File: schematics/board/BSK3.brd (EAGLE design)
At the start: 82 x 100 mm, 19 parts

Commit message: Новые схемы
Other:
- board text added: "BSK3 "Концерн ИТС""
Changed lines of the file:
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@@
 <circle x="41" y="50" radius="16.375" width="2.25" layer="29"/>
 <rectangle x1="10.528" y1="39.862" x2="22.528" y2="56.862" layer="29"/>
-<text x="18.8" y="74" size="1.4224" layer="26" rot="MR0">BUS+</text>
-<text x="68.2" y="74.1" size="1.4224" layer="26" rot="MR0">BUS+</text>
-<text x="68.1" y="24.5" size="1.4224" layer="26" rot="MR0">BUS+</text>
-<text x="18.7" y="24.4" size="1.4224" layer="26" rot="MR0">BUS+</text>
-<text x="27" y="65.6" size="1.4224" layer="26" rot="MR0">BUS-</text>
-<text x="59.6" y="65.5" size="1.4224" layer="26" rot="MR0">BUS-</text>
-<text x="59.6" y="33.2" size="1.4224" layer="26" rot="MR0">BUS-</text>
-<text x="27" y="33" size="1.4224" layer="26" rot="MR0">BUS-</text>
+<text x="13.9" y="68.7" size="1.4224" layer="25" rot="MR45">BUS+</text>
+<text x="72.3" y="72.8" size="1.4224" layer="26" rot="MR315">BUS+</text>
+<text x="60.3" y="24.2" size="1.4224" layer="26" rot="MR225">BUS+</text>
+<text x="17.7" y="20.1" size="1.4224" layer="26" rot="MR135">BUS+</text>
+<text x="22.7" y="60.1" size="1.4224" layer="26" rot="MR45">BUS-</text>
+<text x="62.2" y="62.9" size="1.4224" layer="26" rot="MR315">BUS-</text>
+<text x="52.3" y="32.3" size="1.4224" layer="26" rot="MR225">BUS-</text>
+<text x="26.2" y="28.6" size="1.4224" layer="26" rot="MR135">BUS-</text>
+<text x="80.7" y="41.3" size="1.778" layer="25" rot="R90">BSK3 "Концерн ИТС"</text>
 </plain>
 <attributes>

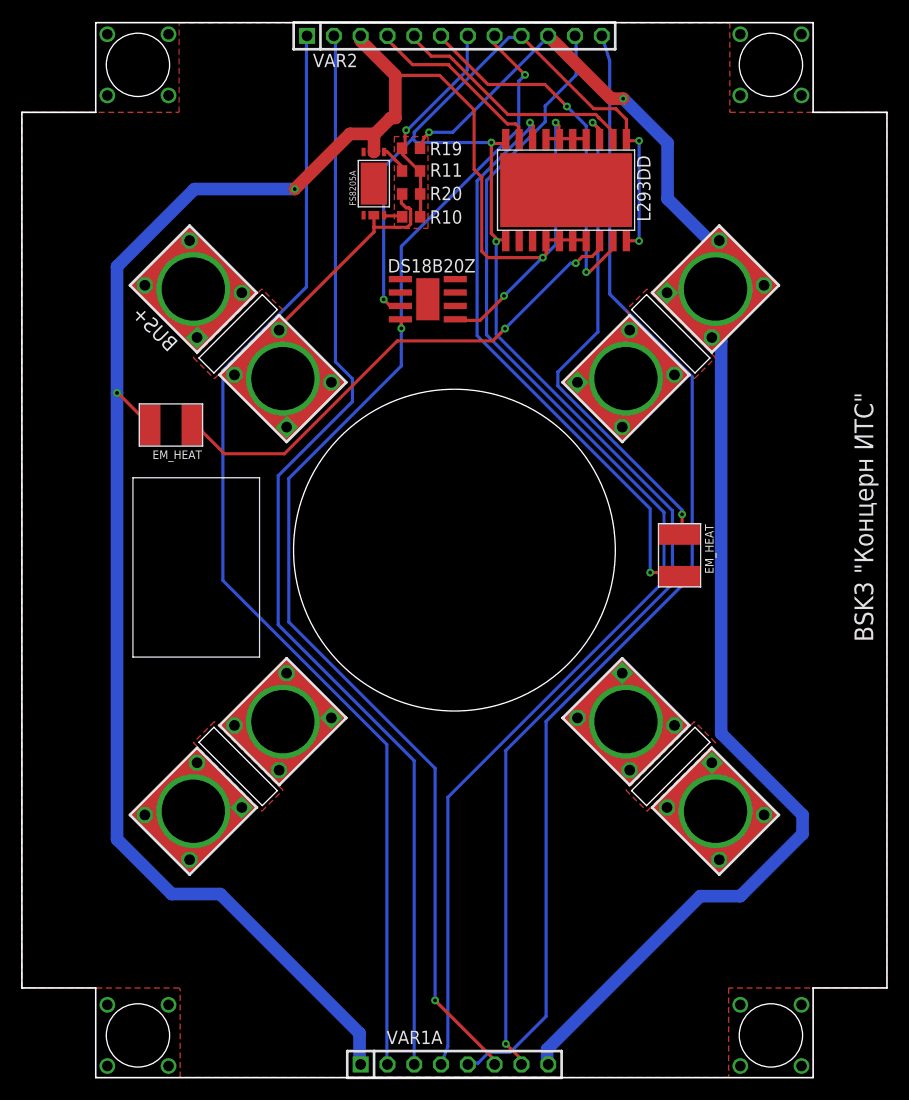
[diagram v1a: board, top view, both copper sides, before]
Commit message: изменен БСК4
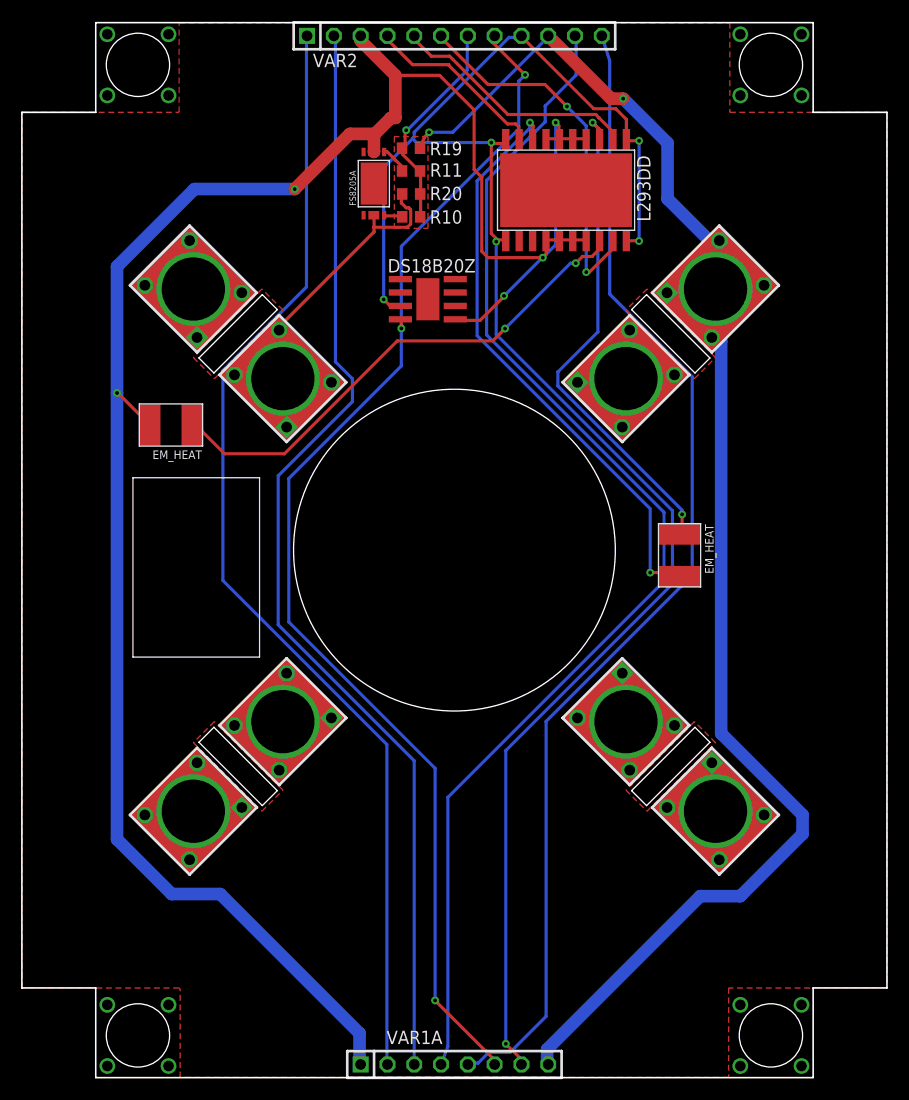
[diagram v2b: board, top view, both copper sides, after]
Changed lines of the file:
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@@
 <circle x="41" y="50" radius="16.375" width="2.25" layer="29"/>
 <rectangle x1="10.528" y1="39.862" x2="22.528" y2="56.862" layer="29"/>
-<text x="13.9" y="68.7" size="1.4224" layer="25" rot="MR45">BUS+</text>
+<text x="13.9" y="68.7" size="1.4224" layer="26" rot="MR45">BUS+</text>
 <text x="72.3" y="72.8" size="1.4224" layer="26" rot="MR315">BUS+</text>
 <text x="60.3" y="24.2" size="1.4224" layer="26" rot="MR225">BUS+</text>
@@
 <text x="52.3" y="32.3" size="1.4224" layer="26" rot="MR225">BUS-</text>
 <text x="26.2" y="28.6" size="1.4224" layer="26" rot="MR135">BUS-</text>
-<text x="80.7" y="41.3" size="1.778" layer="25" rot="R90">BSK3 "Концерн ИТС"</text>
+<text x="53.3" y="9.1" size="1.778" layer="26" rot="MR0">BSK3 "Концерн ИТС"</text>
 </plain>
 <attributes>

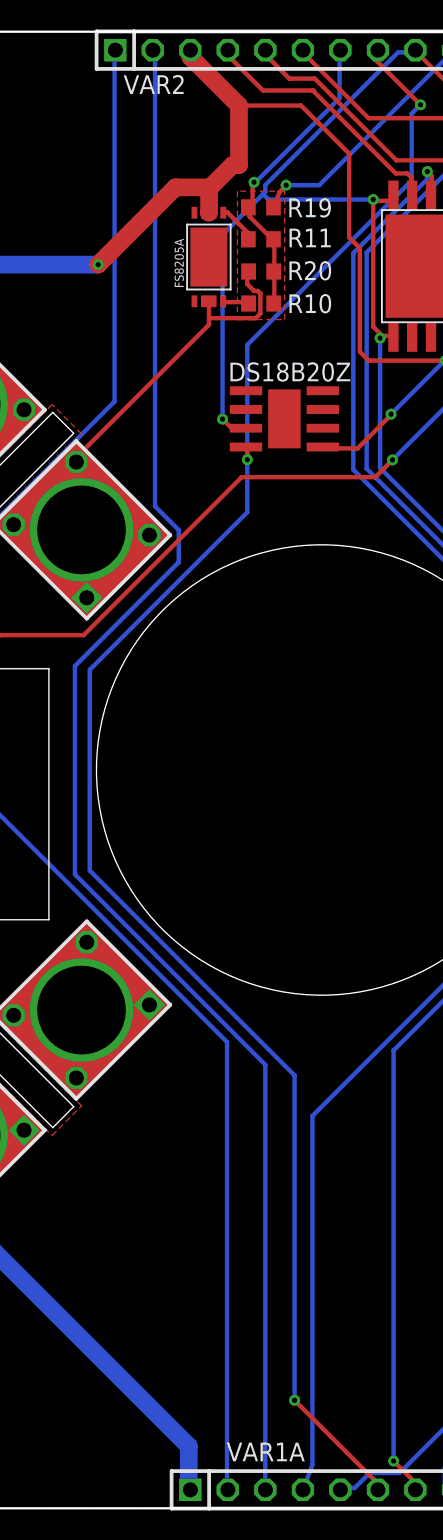
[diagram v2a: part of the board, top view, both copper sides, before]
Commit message: Реструктурированы сигналы коммутации для плат БСК
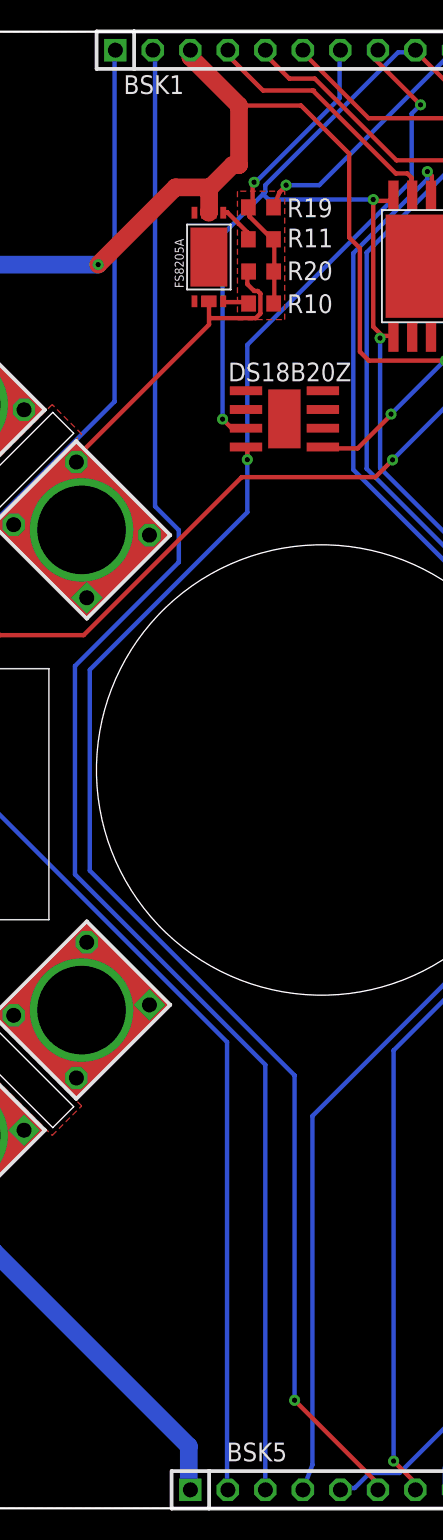
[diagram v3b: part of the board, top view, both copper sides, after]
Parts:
- renumbered VAR1A to BSK5, VAR2 to BSK1
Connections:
- net KEM5 renamed B3_KEM+
- net KEM6 renamed B3_KEM-
- net KEM7 renamed B5_KEM+
- net KEM8 renamed B5_KEM-
- net KHEAT3 renamed B3_KHEAT
- net KHEAT4 renamed B5_KHEAT
- net KVCC3 renamed B3_KVCC
- net KVCC4 renamed B5_KVCC
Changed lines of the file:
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@@
 <element name="U$7" library="CanCubeSat" package="EM_HEAT" value="EM_HEAT" x="14.13" y="61.86" smashed="yes" rot="R180"/>
 <element name="U$8" library="CanCubeSat" package="L293DD" value="L293DD" x="51.58" y="84.12" smashed="yes" rot="R180"/>
-<element name="VAR1A" library="pinheadCS" package="1X08" value="" x="41" y="1.25" smashed="yes">
+<element name="BSK5" library="pinheadCS" package="1X08" value="" x="41" y="1.25" smashed="yes">
 <attribute name="NAME" x="34.5638" y="3.1788" size="1.27" layer="25" ratio="10"/>
 <attribute name="VALUE" x="30.84" y="-1.925" size="1.27" layer="27"/>
 </element>
-<element name="VAR2" library="pinheadCS" package="1X12" value="" x="41" y="98.75" smashed="yes">
+<element name="BSK1" library="pinheadCS" package="1X12" value="" x="41" y="98.75" smashed="yes">
 <attribute name="NAME" x="27.5838" y="95.7788" size="1.27" layer="25" ratio="10"/>
 <attribute name="VALUE" x="25.76" y="95.575" size="1.27" layer="27"/>
@@
 <contactref element="U$8" pad="17"/>
 <contactref element="U$14" pad="67"/>
-<contactref element="VAR1A" pad="1"/>
-<contactref element="VAR2" pad="3"/>
+<contactref element="BSK5" pad="1"/>
+<contactref element="BSK1" pad="3"/>
 <wire x1="33.3756" y1="89.4588" x2="33.3756" y2="87.7824" width="1.2" layer="1"/>
 <wire x1="33.3756" y1="87.7824" x2="33.36" y2="87.74" width="1.2" layer="1"/>
@@
 <contactref element="U$8" pad="11"/>
 <contactref element="U$8" pad="20"/>
-<contactref element="VAR1A" pad="7"/>
-<contactref element="VAR2" pad="9"/>
+<contactref element="BSK5" pad="7"/>
+<contactref element="BSK1" pad="9"/>
 <contactref element="U$5" pad="3"/>
 <wire x1="34.8996" y1="73.152" x2="35.814" y2="73.152" width="0.3" layer="1"/>
@@
 <signal name="1W">
 <contactref element="U$5" pad="4"/>
-<contactref element="VAR1A" pad="6"/>
-<contactref element="VAR2" pad="8"/>
+<contactref element="BSK5" pad="6"/>
+<contactref element="BSK1" pad="8"/>
 <wire x1="35.9664" y1="71.0184" x2="35.9664" y2="71.7804" width="0.3" layer="1"/>
 <wire x1="35.9664" y1="78.7908" x2="35.9664" y2="71.0184" width="0.3" layer="16"/>
@@
 <via x="39.1668" y="7.3152" extent="1-16" drill="0.35"/>
 </signal>
-<signal name="KEM5">
-<contactref element="VAR2" pad="5"/>
+<signal name="B3_KEM+">
+<contactref element="BSK1" pad="5"/>
 <contactref element="U$8" pad="2"/>
 <wire x1="55.9308" y1="89.7588" x2="55.9308" y2="89.0016" width="0.3" layer="1"/>
@@
 <wire x1="37.338" y1="98.6028" x2="37.19" y2="98.75" width="0.3" layer="1"/>
 </signal>
-<signal name="KEM6">
-<contactref element="VAR2" pad="4"/>
+<signal name="B3_KEM-">
+<contactref element="BSK1" pad="4"/>
 <contactref element="U$8" pad="9"/>
 <wire x1="37.0284" y1="96.0168" x2="40.4" y2="96.0168" width="0.3" layer="1"/>
@@
 <wire x1="47.0916" y1="90.1084" x2="47.0916" y2="89.0016" width="0.3" layer="1"/>
 </signal>
-<signal name="KHEAT3">
-<contactref element="VAR2" pad="6"/>
+<signal name="B3_KHEAT">
+<contactref element="BSK1" pad="6"/>
 <contactref element="U$8" pad="19"/>
 <wire x1="55.9308" y1="78.486" x2="55.9308" y2="79.248" width="0.3" layer="1"/>
@@
 <via x="51.6636" y="92.0496" extent="1-16" drill="0.35"/>
 </signal>
-<signal name="KEM7">
-<contactref element="VAR2" pad="2"/>
-<contactref element="VAR1A" pad="3"/>
+<signal name="B5_KEM+">
+<contactref element="BSK1" pad="2"/>
+<contactref element="BSK5" pad="3"/>
 <wire x1="29.718" y1="67.856" x2="29.718" y2="98.6028" width="0.3" layer="16"/>
 <wire x1="31.3276" y1="66.2464" x2="29.718" y2="67.856" width="0.3" layer="16"/>
@@
 <wire x1="37.1856" y1="1.3716" x2="37.19" y2="1.25" width="0.3" layer="16"/>
 </signal>
-<signal name="KEM8">
-<contactref element="VAR2" pad="1"/>
-<contactref element="VAR1A" pad="2"/>
+<signal name="B5_KEM-">
+<contactref element="BSK1" pad="1"/>
+<contactref element="BSK5" pad="2"/>
 <wire x1="26.9748" y1="74.9508" x2="26.9748" y2="98.6028" width="0.3" layer="16"/>
 <wire x1="19.05" y1="67.026" x2="26.9748" y2="74.9508" width="0.3" layer="16"/>
@@
 <wire x1="34.65" y1="1.329709375" x2="34.5948" y2="1.451309375" width="0.3" layer="16"/>
 </signal>
-<signal name="KHEAT4">
-<contactref element="VAR2" pad="11"/>
-<contactref element="VAR1A" pad="4"/>
+<signal name="B5_KHEAT">
+<contactref element="BSK1" pad="11"/>
+<contactref element="BSK5" pad="4"/>
 <wire x1="40.3764" y1="26.57" x2="40.3764" y2="2.9440125" width="0.3" layer="16"/>
 <wire x1="60.8648" y1="47.0584" x2="40.3764" y2="26.57" width="0.3" layer="16"/>
@@
 <wire x1="35.5852" y1="69.8324" x2="44.6324" y2="69.8324" width="0.3" layer="1"/>
 </signal>
-<signal name="KVCC3">
-<contactref element="VAR2" pad="7"/>
+<signal name="B3_KVCC">
+<contactref element="BSK1" pad="7"/>
 <contactref element="R10" pad="1"/>
 <contactref element="R11" pad="1"/>
@@
 <via x="36.4236" y="89.8064" extent="1-16" drill="0.35"/>
 </signal>
-<signal name="KVCC4">
-<contactref element="VAR2" pad="12"/>
-<contactref element="VAR1A" pad="5"/>
+<signal name="B5_KVCC">
+<contactref element="BSK1" pad="12"/>
+<contactref element="BSK5" pad="5"/>
 <wire x1="43.234" y1="1.3716" x2="42.3672" y2="1.3716" width="0.3" layer="16"/>
 <wire x1="44.2532" y1="2.3908" x2="43.234" y2="1.3716" width="0.3" layer="16"/>
@@
 <signal name="BUS+">
 <contactref element="R19" pad="2"/>
-<contactref element="VAR1A" pad="8"/>
-<contactref element="VAR2" pad="10"/>
+<contactref element="BSK5" pad="8"/>
+<contactref element="BSK1" pad="10"/>
 <contactref element="U$3" pad="1"/>
 <contactref element="U$3" pad="2"/>

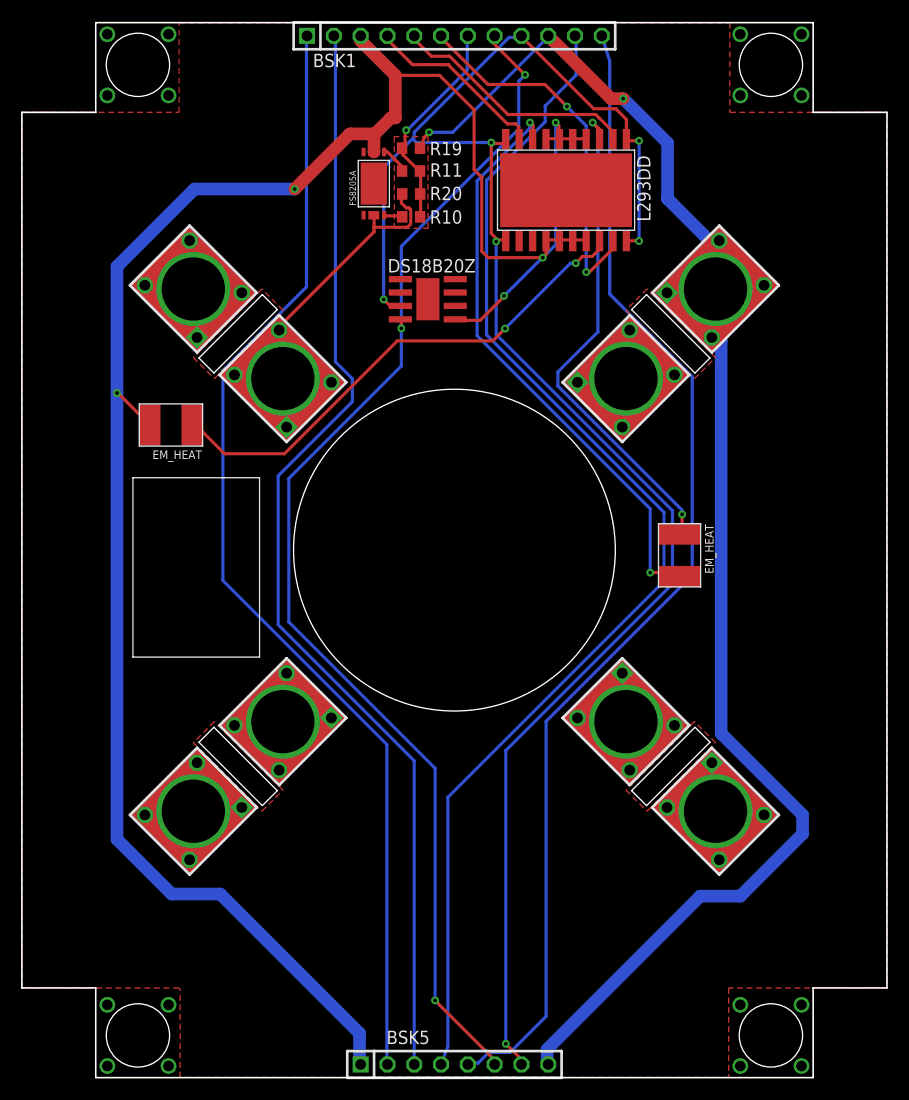
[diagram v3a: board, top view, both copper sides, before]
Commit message: Добавлены светодиоды на платы БСК
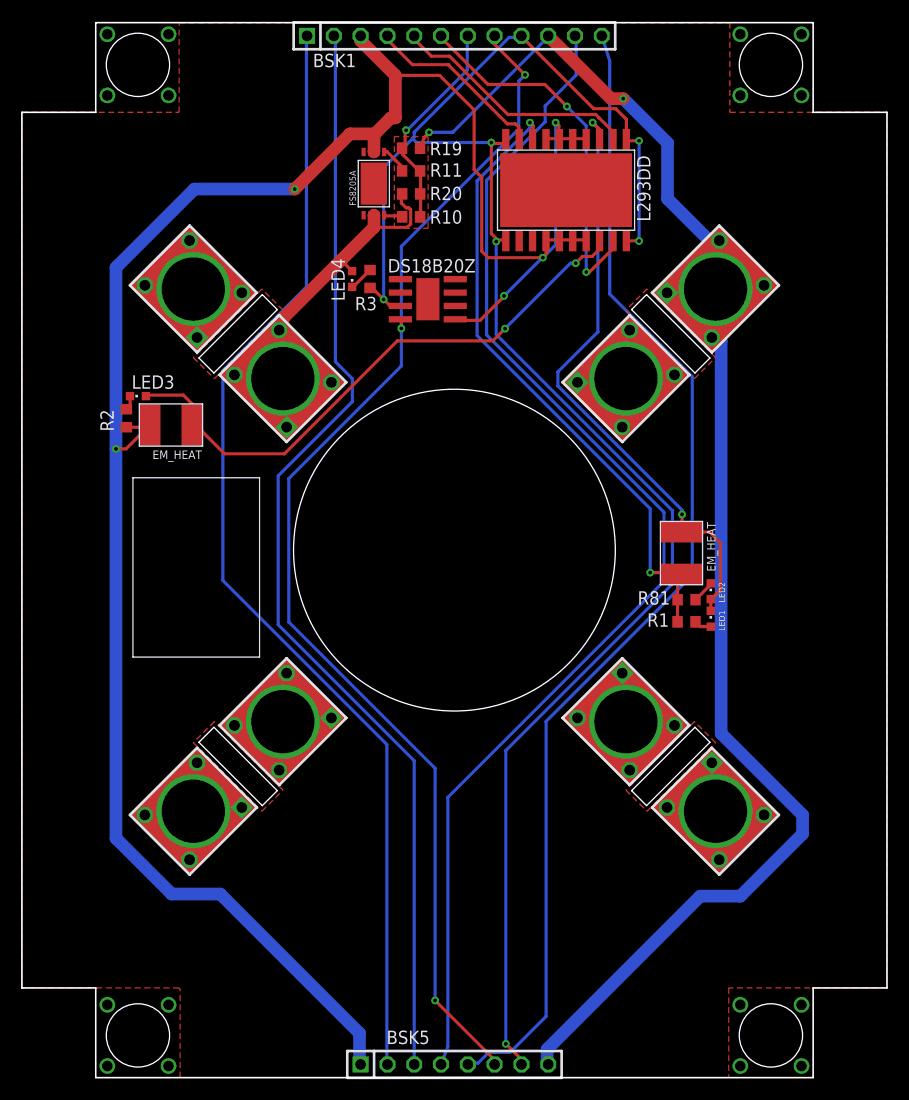
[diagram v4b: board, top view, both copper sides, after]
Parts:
- added LED1, LED2, LED3, LED4: (no value), led:CHIPLED_0603
- added R1, R2, R3, R81: 2k, resistor:R0603
- moved U$6 0.28 mm to (62.5, 49.7)
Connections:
- new net N$4: LED2.C, R81.2
- new net N$5: LED1.A, R1.2
- new net N$6: LED3.C, R2.1
- new net N$7: LED4.C, R3.2
- net 5V: now also R3.1
- net BUS-: now also LED4.A
- net GND: now also R2.2
- net N$1: now also LED1.C, LED2.A
- net N$2: now also R1.1, R81.1
- net N$3: now also LED3.A
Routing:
- net N$1: track 47.6 -> 58.3 mm
- net N$3: track 48.6 -> 55.3 mm
- net BUS-: track 41.0 -> 46.8 mm
- net N$2: track 56.2 -> 61.5 mm
- net N$7: track 0.00 -> 2.36 mm
- net N$4: track 0.00 -> 2.15 mm
- net GND: track 199.6 -> 201.7 mm
- net 5V: track 171.8 -> 173.5 mm
- net N$5: track 0.00 -> 1.64 mm
- net N$6: track 0.00 -> 1.39 mm

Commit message: Разведены платы БСК2-5
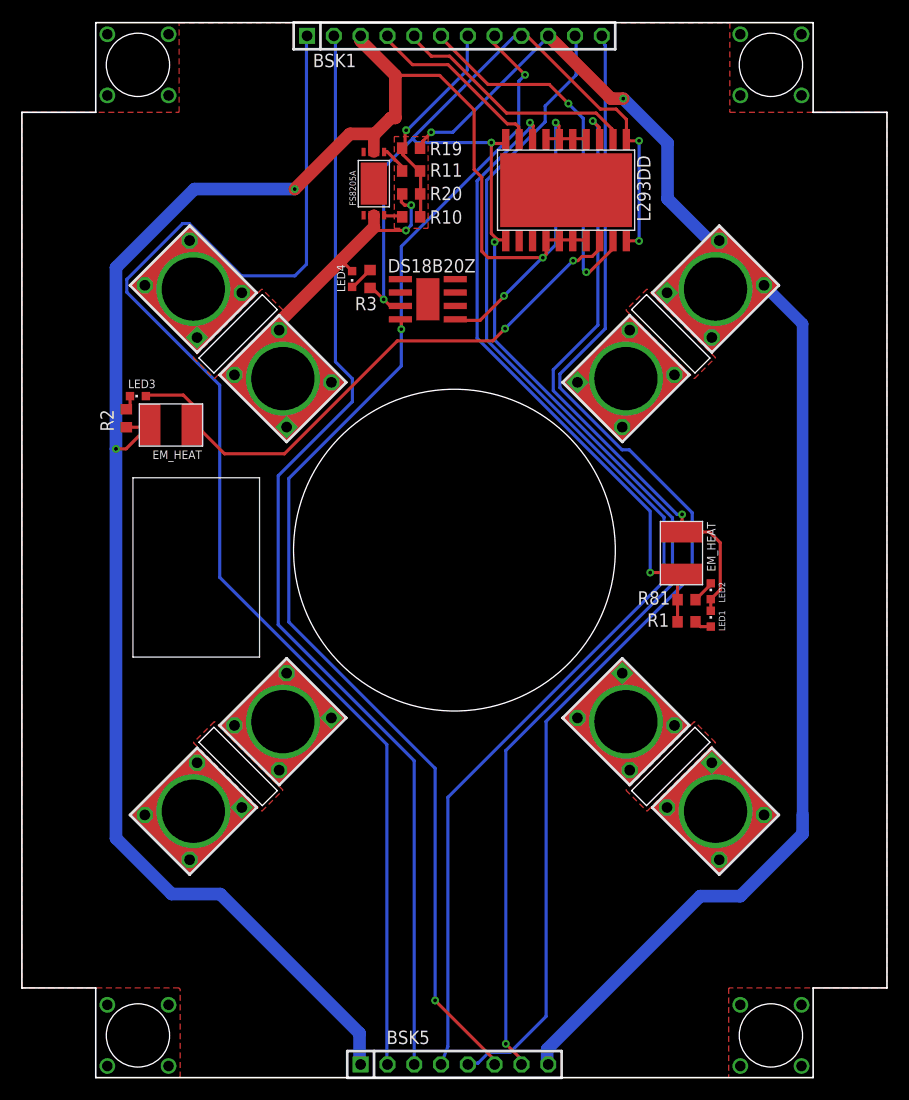
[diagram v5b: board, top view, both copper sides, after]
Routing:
- net B5_KEM-: track 107.2 -> 128.0 mm
- net B5_KVCC: track 111.4 -> 115.4 mm
- net BUS-: track 46.8 -> 42.9 mm, vias 0 -> 2
- net BUS+: track 148.7 -> 150.9 mm
- net N$1: track 58.3 -> 59.2 mm
- net N$2: track 61.5 -> 61.0 mm
